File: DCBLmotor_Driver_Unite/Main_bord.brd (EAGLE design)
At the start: 80 x 66 mm, 72 parts, among them CN1 DF11-16DP-2DSA, CN2 DF11-16DP-2DSA, CN3 DF11-4DP-2DSR, CN4 HIF3FC-10PA-2.54DSA(71), CN5 HIF3FC-10PA-2.54DSA(71), CN6 0430450612, CN7 0430450612, CN8 BM11B-SRSS-TB, IC1 TMPM370FYFG, IC2 MCP2561FD-E/MF, IC3 AM26C32CD, IC4 AM26C32CD, IC5 LTC2862A, SW1 CVS-02TB, SW2 EVQ-PE104K

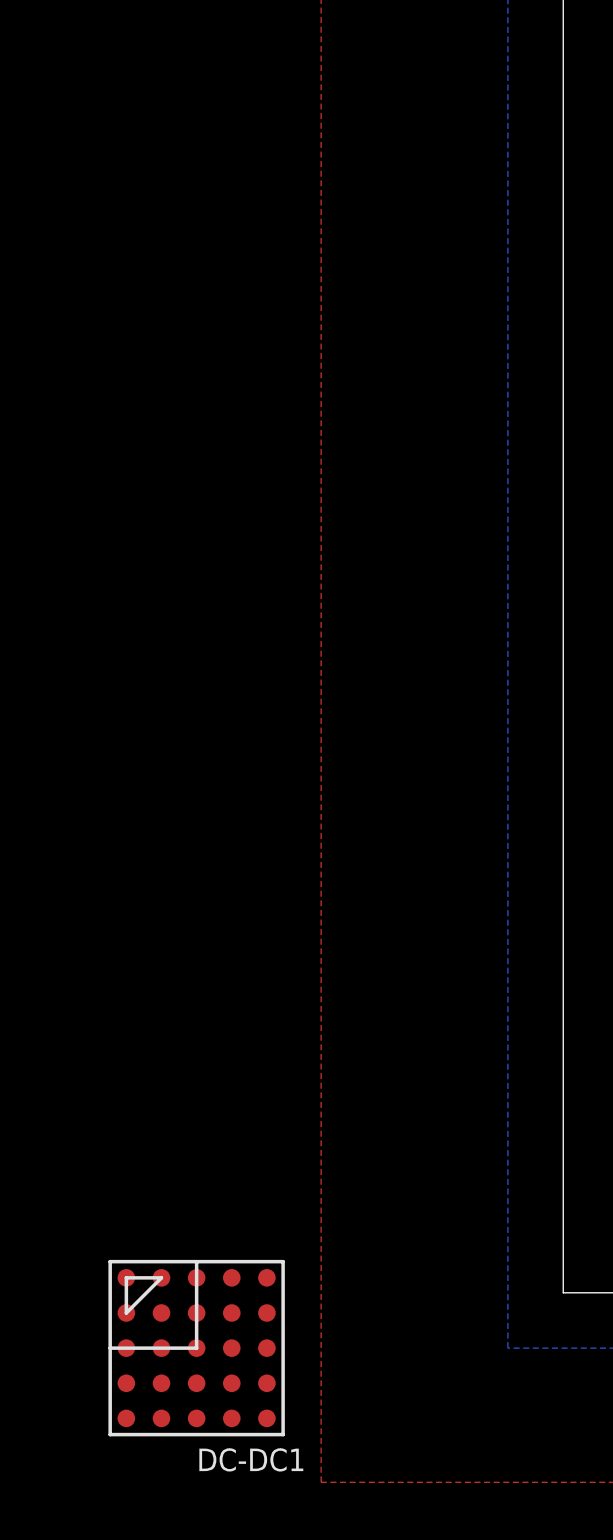
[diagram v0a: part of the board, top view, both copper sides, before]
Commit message: Add LTM4623
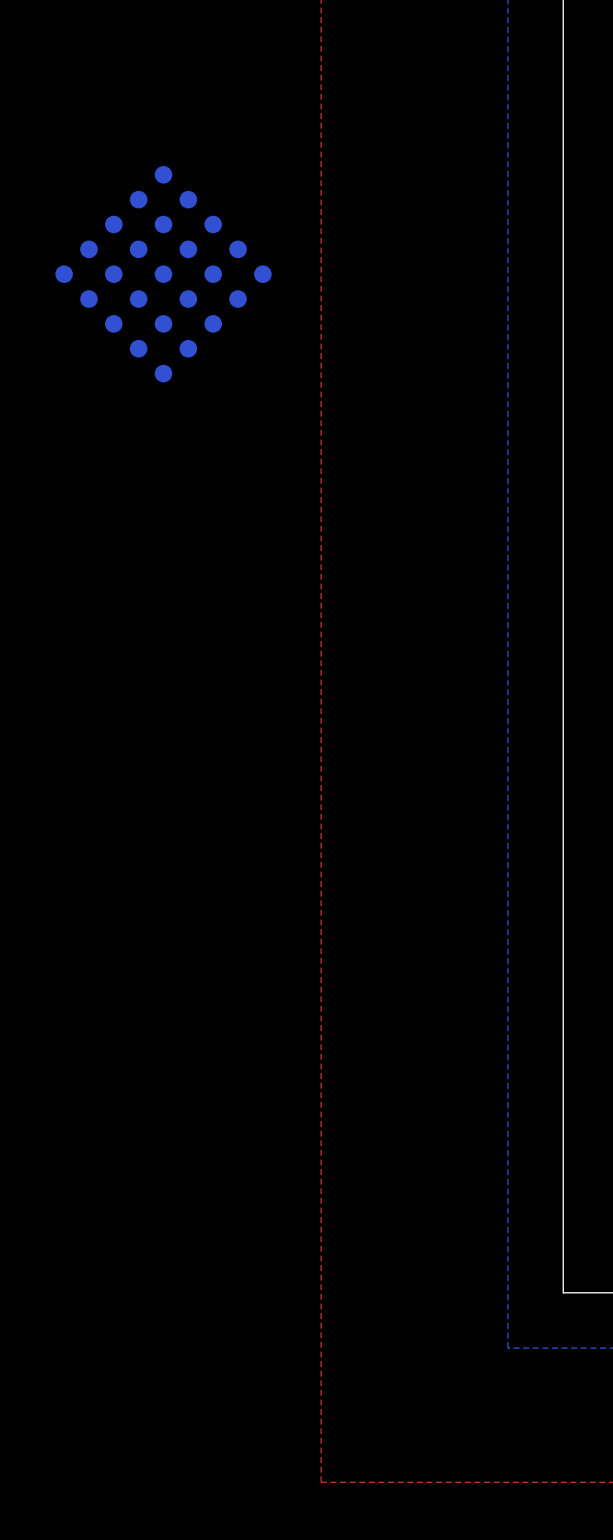
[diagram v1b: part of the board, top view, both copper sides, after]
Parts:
- moved DC-DC1 38.8 mm to (-16.4, 67.8), flipped to the bottom, turned to 45 degrees
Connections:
- net +5V: now also C7.P$1, DC-DC1.C1, DC-DC1.D1, DC-DC1.D2, DC-DC1.E1, DC-DC1.E2
- net GND: now also DC-DC1.B3, DC-DC1.B4, DC-DC1.C3, DC-DC1.D3, DC-DC1.D4, DC-DC1.E3
- net VCC: no longer C7.P$1
- net VDD: now also DC-DC1.A3, DC-DC1.C5, DC-DC1.D5, DC-DC1.E5
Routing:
- net VCC: track 14.0 -> 0.83 mm, vias 1 -> 0
- net +5V: track 69.0 -> 82.2 mm, vias 19 -> 20
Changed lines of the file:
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@@
 <element name="CN10" library="jst-xh" package="B2B-XH-A" value="" x="3.925" y="39"/>
 <element name="C5" library="KEMET" package="T356" value="T356L107K016AT" x="5.225" y="47.5"/>
-<element name="DC-DC1" library="LT" package="LGA-25_STD" value="LTM4623IY" x="-15.25" y="29"/>
+<element name="DC-DC1" library="LT" package="LGA-25_STD" value="LTM4623IY" x="-16.4474875" y="67.81464375" smashed="yes" rot="MR45">
+<attribute name="NAME" x="-19.590578125" y="64.671553125" size="0.8128" layer="22" rot="MR45"/>
+</element>
 </elements>
 <signals>
@@
 <wire x1="2" y1="66.575" x2="2" y2="69.8" width="0.2" layer="1"/>
 <wire x1="11.95" y1="65.3" x2="12.325" y2="64.925" width="0.1524" layer="1"/>
+<contactref element="DC-DC1" pad="C3"/>
+<contactref element="DC-DC1" pad="B3"/>
+<contactref element="DC-DC1" pad="D3"/>
+<contactref element="DC-DC1" pad="E3"/>
+<contactref element="DC-DC1" pad="D4"/>
+<contactref element="DC-DC1" pad="B4"/>
 <wire x1="73.2" y1="85.9" x2="75.65" y2="88.55" width="0" layer="19" extent="1-1"/>
 <wire x1="71.5" y1="82.3" x2="73.2" y2="85.9" width="0" layer="19" extent="1-1"/>
@@
 <wire x1="15.15" y1="33.5" x2="5.175" y2="39" width="0" layer="19" extent="1-1"/>
 <wire x1="32.8" y1="33.5" x2="22.75" y2="43.65" width="0" layer="19" extent="1-1"/>
+<wire x1="-15.5494625" y1="66.916615625" x2="0.9" y2="62.2" width="0" layer="19" extent="1-16"/>
+<wire x1="-16.4474875" y1="67.81464375" x2="-15.5494625" y2="66.916615625" width="0" layer="19" extent="16-16"/>
+<wire x1="-17.345515625" y1="68.71266875" x2="-16.4474875" y2="67.81464375" width="0" layer="19" extent="16-16"/>
+<wire x1="-18.243540625" y1="69.61069375" x2="-17.345515625" y2="68.71266875" width="0" layer="19" extent="16-16"/>
+<wire x1="-18.243540625" y1="67.81464375" x2="-17.345515625" y2="68.71266875" width="0" layer="19" extent="16-16"/>
+<wire x1="-16.4474875" y1="66.018590625" x2="-15.5494625" y2="66.916615625" width="0" layer="19" extent="16-16"/>
 </signal>
 <signal name="N$7">
@@
 </signal>
 <signal name="VCC">
-<contactref element="C7" pad="P$1"/>
 <contactref element="R2" pad="P$1"/>
 <wire x1="10.3" y1="72.7" x2="10.3" y2="72.15" width="0.1524" layer="1"/>
 <wire x1="10.3" y1="72.15" x2="10.5" y2="71.95" width="0.1524" layer="1"/>
-<wire x1="10.55" y1="71.7" x2="10.5" y2="71.7" width="0.1524" layer="16"/>
-<via x="10.5" y="71.7" extent="1-16" drill="0.2"/>
-<wire x1="21.58" y1="67.3" x2="20.31" y2="67.3" width="0.508" layer="16"/>
-<wire x1="20.31" y1="67.3" x2="18.014140625" y2="67.3" width="0.508" layer="16"/>
-<wire x1="18.014140625" y1="67.3" x2="14.5" y2="67.3" width="0.508" layer="16"/>
-<wire x1="10.5" y1="71.3" x2="10.5" y2="71.7" width="0.508" layer="16"/>
-<wire x1="14.5" y1="67.3" x2="12.575" y2="69.225" width="0.508" layer="16"/>
-<wire x1="12.575" y1="69.225" x2="10.5" y2="71.3" width="0.508" layer="16"/>
-<wire x1="10.55" y1="71.7" x2="10.5" y2="71.95" width="0" layer="19" extent="1-16"/>
 </signal>
 <signal name="VDD">
@@
 <wire x1="2.685" y1="47.5" x2="2.685" y2="50.285" width="1.27" layer="2"/>
 <wire x1="2.685" y1="50.285" x2="4.65" y2="52.25" width="1.27" layer="2"/>
+<contactref element="DC-DC1" pad="D5"/>
+<contactref element="DC-DC1" pad="E5"/>
+<contactref element="DC-DC1" pad="C5"/>
+<contactref element="DC-DC1" pad="A3"/>
+<wire x1="-18.243540625" y1="66.018590625" x2="-14.6514375" y2="66.018590625" width="0" layer="19" extent="16-16"/>
+<wire x1="-19.141565625" y1="66.916615625" x2="-18.243540625" y2="66.018590625" width="0" layer="19" extent="16-16"/>
+<wire x1="-20.039590625" y1="67.81464375" x2="-19.141565625" y2="66.916615625" width="0" layer="19" extent="16-16"/>
+<wire x1="4.65" y1="60.3" x2="-14.6514375" y2="66.018590625" width="0" layer="19" extent="2-16"/>
 </signal>
 <signal name="N$16">
@@
 <wire x1="39.3" y1="92.85" x2="39.2" y2="92.75" width="0.4064" layer="3"/>
 <wire x1="39.2" y1="92.75" x2="39.3" y2="92.95" width="0.4064" layer="3"/>
+<contactref element="DC-DC1" pad="D2"/>
+<contactref element="DC-DC1" pad="E1"/>
+<contactref element="DC-DC1" pad="E2"/>
+<contactref element="DC-DC1" pad="C1"/>
+<contactref element="DC-DC1" pad="D1"/>
+<contactref element="C7" pad="P$1"/>
+<wire x1="10.55" y1="71.7" x2="10.5" y2="71.7" width="0.1524" layer="16"/>
+<via x="10.5" y="71.7" extent="1-16" drill="0.2"/>
+<wire x1="21.58" y1="67.3" x2="20.31" y2="67.3" width="0.508" layer="16"/>
+<wire x1="20.31" y1="67.3" x2="18.014140625" y2="67.3" width="0.508" layer="16"/>
+<wire x1="18.014140625" y1="67.3" x2="14.5" y2="67.3" width="0.508" layer="16"/>
+<wire x1="10.5" y1="71.3" x2="10.5" y2="71.7" width="0.508" layer="16"/>
+<wire x1="14.5" y1="67.3" x2="12.575" y2="69.225" width="0.508" layer="16"/>
+<wire x1="12.575" y1="69.225" x2="10.5" y2="71.3" width="0.508" layer="16"/>
 <wire x1="56.75" y1="78.85" x2="61.7" y2="79.4" width="0" layer="19" extent="1-1"/>
 <wire x1="56.7" y1="64.15" x2="56.7" y2="78" width="0" layer="19" extent="1-1"/>
@@
 <wire x1="59.7" y1="39.2" x2="59.3" y2="51.1" width="0" layer="19" extent="1-1"/>
 <wire x1="26.1069375" y1="64.35334375" x2="38.4" y2="55.5" width="0" layer="19" extent="16-16"/>
-<wire x1="20.60668125" y1="63.63179375" x2="23.75" y2="65.05" width="0" layer="19" extent="16-16"/>
+<wire x1="21.58" y1="67.3" x2="23.75" y2="65.05" width="0" layer="19" extent="16-16"/>
+<wire x1="19.05" y1="65.05" x2="18.014140625" y2="67.3" width="0" layer="19" extent="16-16"/>
+<wire x1="15.742853125" y1="71.157146875" x2="12.575" y2="69.225" width="0" layer="19" extent="16-16"/>
 <wire x1="29.962128125" y1="71.1" x2="28.349496875" y2="67.318196875" width="0" layer="19" extent="16-16"/>
-<wire x1="23.4" y1="77" x2="27.895446875" y2="73.414453125" width="0" layer="19" extent="16-16"/>
-<wire x1="17.830653125" y1="73.3947875" x2="21.745525" y2="77.28276875" width="0" layer="19" extent="16-16"/>
-<wire x1="12.425" y1="78.775" x2="17.830653125" y2="73.3947875" width="0" layer="19" extent="1-16"/>
+<wire x1="21.745525" y1="77.28276875" x2="17.830653125" y2="73.3947875" width="0" layer="19" extent="16-16"/>
+<wire x1="12.425" y1="78.775" x2="10.55" y2="71.7" width="0" layer="19" extent="1-16"/>
 <wire x1="12.5" y1="87.85" x2="12.15" y2="83.05" width="0" layer="19" extent="1-1"/>
 <wire x1="13.85" y1="56.05" x2="20.60668125" y2="63.39795" width="0" layer="19" extent="1-16"/>
 <wire x1="11.85" y1="51.125" x2="13.26715" y2="56.05" width="0" layer="19" extent="1-1"/>
 <wire x1="36.45" y1="92.65" x2="22.9398375" y2="77.926484375" width="0" layer="19" extent="1-16"/>
+<wire x1="-14.6514375" y1="69.61069375" x2="10.5" y2="71.3" width="0" layer="19" extent="16-16"/>
+<wire x1="-15.5494625" y1="70.50871875" x2="-14.6514375" y2="69.61069375" width="0" layer="19" extent="16-16"/>
+<wire x1="-16.4474875" y1="71.40674375" x2="-15.5494625" y2="70.50871875" width="0" layer="19" extent="16-16"/>
+<wire x1="-16.4474875" y1="69.61069375" x2="-15.5494625" y2="70.50871875" width="0" layer="19" extent="16-16"/>
+<wire x1="-17.345515625" y1="70.50871875" x2="-16.4474875" y2="71.40674375" width="0" layer="19" extent="16-16"/>
 </signal>
 <signal name="AGND">

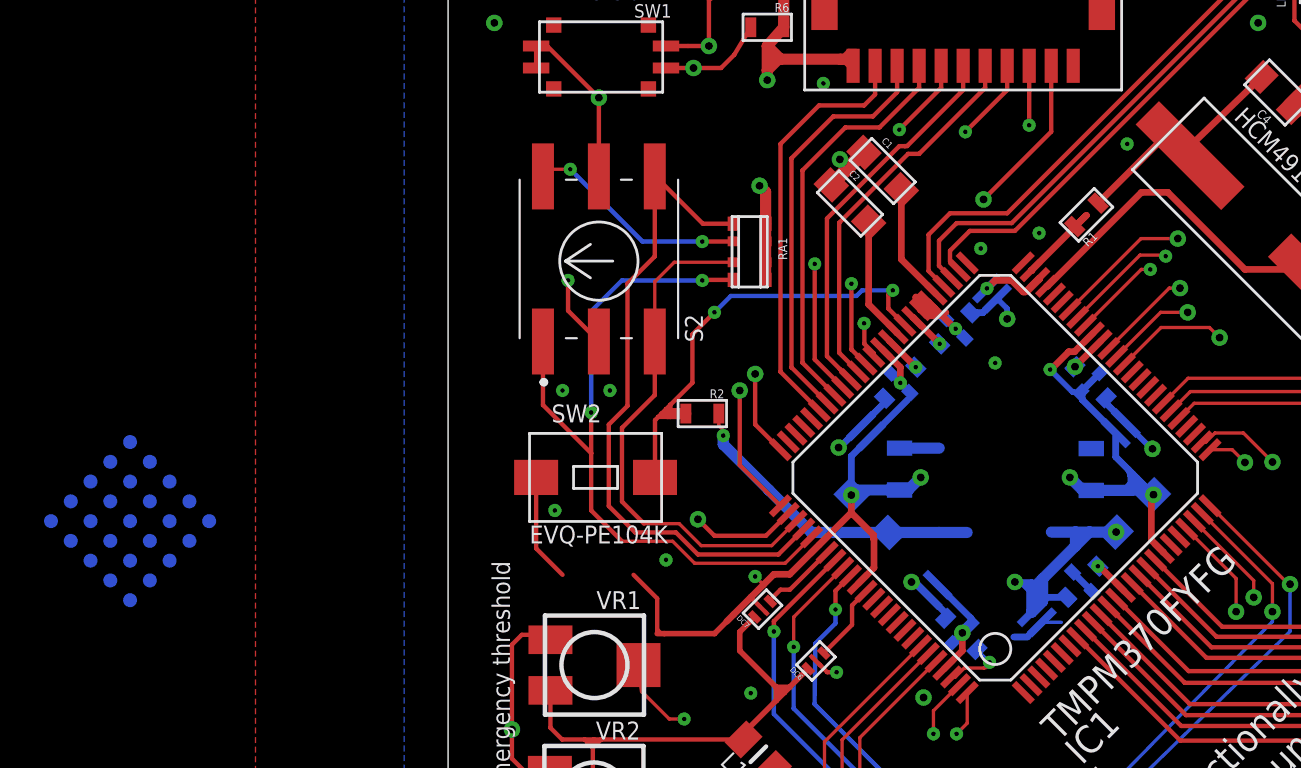
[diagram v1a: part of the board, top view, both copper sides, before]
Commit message: Repless to LTM4623
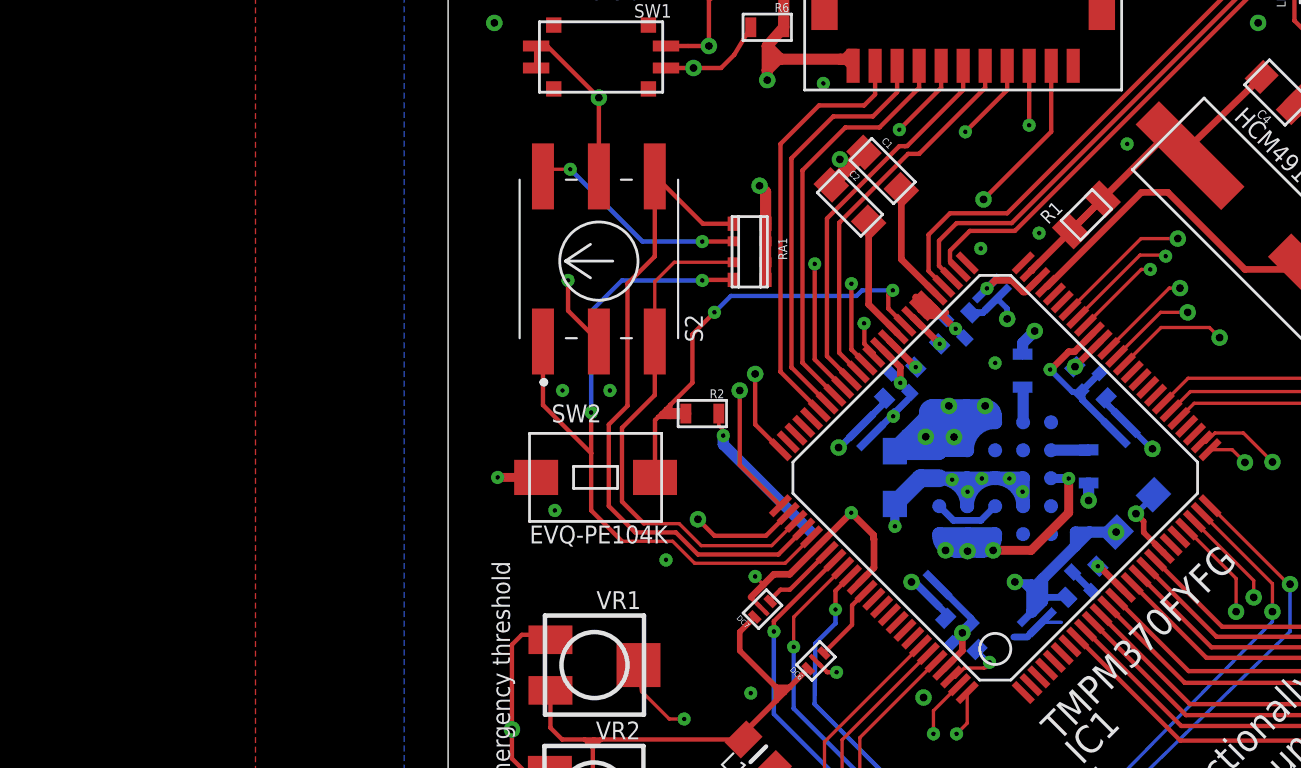
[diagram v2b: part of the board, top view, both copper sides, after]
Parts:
- removed RS1: KTR10EZPF1332, ROHM:KTR10
- removed RS2: KTR10EZPF8251, ROHM:KTR10
- added C6: CGA3E2X7R1H104K080AA, TDK:0603
- added R3: ERA-3AEB8251V, Panasonic:0603
- R1: value CRCW060382R0JNEA -> 5106; device VISHAY:0603 -> Keystone:5106JUMP_0805
- moved DC-DC1 39.3 mm to (22.9, 69.8), turned to 0 degrees
- moved C7 3.71 mm to (18.3, 71.0), turned to 270 degrees
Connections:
- removed net N$10: RS2.P$1
- new net N$12: C6.P$1, DC-DC1.A2
- new net N$45: DC-DC1.C4, DC-DC1.E4
- net GND: now also C6.P$2, R3.P$1; no longer RS1.P$2, RS2.P$2
- net N$7: now also DC-DC1.B1, R3.P$2; no longer RS1.P$1
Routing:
- net +5V: track 82.2 -> 104.6 mm, vias 20 -> 24
- net GND: track 142.5 -> 124.7 mm, vias 93 -> 101
- net VDD: track 48.0 -> 60.3 mm, vias 0 -> 4
- net N$45: track 0.00 -> 3.08 mm
- net N$11: track 11.0 -> 12.8 mm
- net N$12: track 0.00 -> 1.71 mm

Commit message: TEMP Chenge MCU
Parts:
- removed C7, C8: C2012JB0J476M125AC, TDK:C2012
- removed CN10: (no value), jst-xh:B2B-XH-A
- removed CN2: DF11-16DP-2DSA, Hirose:DF11-16DP-2D
- removed CN3: DF11-4DP-2DSR, Hirose:DF11_4DP-2D
- removed CN4, CN5: HIF3FC-10PA-2.54DSA(71), Hirose:HIF3FC-10PA
- removed CN6, CN7: 0430450612, Molex:0430450612
- removed CR10, CR11, CR8: NSI50010YT1G, ON Semiconductor:SOD-123
- removed DC-DC1: LTM4623IY, LT:LGA-25_STD
- removed DC10, DC11, DC12, DC13, DC14: YFF21PC1E104MT000N, TDK:YFF21PC
- removed IC3, IC4: AM26C32CD, AM26C32CD:SOIC127P600X175-16N
- removed LED2: CL-340T-SD-T, Citizen:CL-340
- removed R1: 5106, Keystone:5106JUMP_0805
- removed R3: ERA-3AEB8251V, Panasonic:0603
- removed R4, R5: CRCW060360R4FKEA, VISHAY:0603
- removed VR1: 3314J-1-104E, Bourns:3314J-1
- C3, C4: value CGA1A2C0G1E180J030BA -> GRM0225C1E120JA03L; device TDK:CC0603 -> murata:0402
- C5: value T356L107K016AT -> GRM035R60J475ME15D; device KEMET:T356 -> murata:0603
- C6: value CGA3E2X7R1H104K080AA -> GRM035R60J475ME15D; device TDK:0603 -> murata:0603
- CN1: value DF11-16DP-2DSA -> FX23L-20S-0.5SV; device Hirose:DF11-16DP-2D -> FX23L-20S-0.5SV:FX23L-20S-0.5SV
- DC9: value YFF21PC1E104MT000N -> YFF15PC1C104MT000N; device TDK:YFF21PC -> TDK:YFF15PC
- IC2: value MCP2561FD-E/MF -> TMPM373FWDUG; device MicroChip:8-DFN -> TMPM373FWDUG:QFP50P900X900X160-48N
- XTAL1: value HCM4910000000ABJT -> ABM8AIG-10.000MHZ-12-2Z-T3; device Citizen:HCM49 -> Abracon:ABM8AIG
- moved C3 77.5 mm to (7.30, 13.0), turned to 180 degrees
- moved C4 75.3 mm to (6.30, 18.4), turned to 0 degrees
- moved XTAL1 69.9 mm to (6.80, 15.7), turned to 270 degrees
- moved DC9 53.9 mm to (24.1, 22.2), flipped to the bottom, turned to 180 degrees
- moved C6 52.0 mm to (20.8, 18.7), turned to 180 degrees
- moved DC8 41.7 mm to (20.4, 22.2), flipped to the bottom
- moved IC2 40.9 mm to (22.3, 20.0)
- moved CN1 32.2 mm to (20.4, 7.80), flipped to the bottom
- moved C5 31.4 mm to (20.8, 20.2), flipped to the bottom, turned to 180 degrees
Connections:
- removed net 1SD: CN1.P$2
- removed net 1_A1: CN4.P$5, IC3.1
- removed net 1_A2: CN4.P$6, IC3.2
- removed net 1_B1: CN4.P$7, IC3.6
- removed net 1_B2: CN4.P$8, IC3.7
- removed net 1_I1: CN4.P$9, IC3.10
- removed net 1_I2: CN4.P$10, IC3.9
- removed net 2SD: CN2.P$2
- removed net 2_A1: CN5.P$5, IC4.1
- removed net 2_A2: CN5.P$6, IC4.2
- removed net 2_B1: CN5.P$7, IC4.6
- removed net 2_B2: CN5.P$8, IC4.7
- removed net CANH: CN3.P$1, IC2.P$7, R4.P$1
- removed net CANL: CN3.P$3, IC2.P$6, R5.P$1
- removed net N$12: C6.P$1, DC-DC1.A2
- removed net N$28: DC10.P$2, IC4.16
- removed net N$29: DC9.P$2, IC3.16
- removed net N$30: CN5.P$2, DC12.P$2
- removed net N$31: CN4.P$2, DC11.P$2
- removed net N$32: CN6.P$5, DC13.P$2
- removed net N$33: CN7.P$5, DC14.P$2
- removed net N$35: CN5.P$9, IC4.10
- removed net N$36: CN5.P$10, IC4.9
- removed net N$40: CR8.P$A, LED2.P$4
- removed net N$41: CR11.P$A, LED2.P$5
- removed net N$42: CR10.P$A, LED2.P$6
- removed net N$45: DC-DC1.C4, DC-DC1.E4
- removed net SPLT: CN3.P$2, IC2.P$5, R4.P$2, R5.P$2
- removed net VDD: C5.P$+, CN10.1, DC-DC1.A3, DC-DC1.C5, DC-DC1.D5, DC-DC1.E5
- new net DVSS(1): IC2.10
- new net DVSS(2): IC2.28
- new net N$10: DC8.P$1, IC2.26
- new net RVDD5: IC2.32
- net +5V: no longer C7.P$1, C8.P$1, DC-DC1.C1, DC-DC1.D1, DC-DC1.D2, DC-DC1.E1, DC-DC1.E2, DC10.P$1, DC11.P$1, DC12.P$1, DC13.P$1, DC14.P$1, DC8.P$2, DC9.P$1, LED2.P$1, LED2.P$2, LED2.P$3
- net 1U_H: no longer CN1.P$7
- net 1U_L: no longer CN1.P$8
- net 1V_H: no longer CN1.P$3
- net 1V_L: no longer CN1.P$4
- net 1W_H: no longer CN1.P$5
- net 1W_L: no longer CN1.P$6
- net 2U_H: no longer CN2.P$7
- net 2U_L: no longer CN2.P$8
- net 2V_H: no longer CN2.P$3
- net 2V_L: no longer CN2.P$4
- net 2W_H: no longer CN2.P$5
- net 2W_L: no longer CN2.P$6
- net AVDD: no longer VR1.P$1
- net CU1_1: no longer CN1.P$15
- net CU1_2: no longer CN1.P$14
- net CU1_3: no longer CN1.P$13
- net CU2_1: no longer CN2.P$15
- net CU2_2: no longer CN2.P$14
- net CU2_3: no longer CN2.P$13
- net CVR2: no longer VR1.P$2
- net ENC_A-1: no longer CN6.P$1, IC3.3
- net ENC_A-2: no longer CN7.P$1, IC4.3
- net ENC_B-1: no longer CN6.P$2, IC3.5
- net ENC_B-2: no longer CN7.P$2, IC4.5
- net ENC_Z-1: no longer CN6.P$3, IC3.11
- net ENC_Z-2: no longer CN7.P$3, IC4.11
- net GND: no longer C5.P$-, C6.P$2, C7.P$2, C8.P$2, CN10.2, CN4.P$3, CN5.P$3, CN6.P$4, CN7.P$4, DC-DC1.B3, DC-DC1.B4, DC-DC1.C3, DC-DC1.D3, DC-DC1.D4, DC-DC1.E3, DC10.GND1, DC10.GND2, DC11.GND1, DC11.GND2, DC12.GND1, DC12.GND2, DC13.GND1, DC13.GND2, DC14.GND1, DC14.GND2, DC8.P$3, DC8.P$4, DC9.GND1, DC9.GND2, IC2.P$2, IC2.P$9, IC3.8, IC4.8, R3.P$1, VR1.P$3
- net LED2_1: no longer CR10.P$C
- net LED2_2: no longer CR11.P$C
- net LED2_3: no longer CR8.P$C
- net N$11: now also DC9.P$2, IC2.11; no longer C4.P$1, R1.P$2, XTAL1.P$2
- net N$6: now also C5.P$1, IC2.30; no longer DC8.P$1, IC2.P$3
- net N$7: now also C6.P$1, IC2.33; no longer DC-DC1.B1, R3.P$2
- net RX0: no longer IC2.P$4
- net STBY: no longer IC2.P$8
- net TX0: no longer IC2.P$1
- net X1: now also C4.P$1, IC2.27; no longer C3.P$1
- net X2: now also C3.P$1, IC2.29, XTAL1.P$3; no longer R1.P$1
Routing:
- net VDD: track 60.3 -> 0.00 mm, vias 4 -> 0
- net ENC_B-2: track 104.4 -> 50.1 mm
- net ENC_A-2: track 103.2 -> 51.3 mm
- net GND: track 124.7 -> 75.2 mm, vias 101 -> 79
- net +5V: track 104.6 -> 57.5 mm, vias 24 -> 13
- net X2: track 4.64 -> 20.5 mm
- net CANH: track 15.1 -> 0.00 mm, vias 1 -> 0
- net X1: track 22.2 -> 36.9 mm
- net N$36: track 13.5 -> 0.00 mm, vias 1 -> 0
- net 1_I2: track 13.4 -> 0.00 mm, vias 1 -> 0
- net N$11: track 12.8 -> 0.00 mm
- net 2_A2: track 12.2 -> 0.00 mm
- net N$35: track 10.4 -> 0.00 mm
- net 1_I1: track 10.3 -> 0.00 mm, vias 1 -> 0
- net 1W_L: track 38.7 -> 28.6 mm
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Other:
- board size 80 x 66 mm -> 33 x 46 mm
